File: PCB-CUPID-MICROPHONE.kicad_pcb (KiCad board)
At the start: 2 copper layers, 25.4 x 22.9 mm, 16 parts, among them J2 Conn_01x05

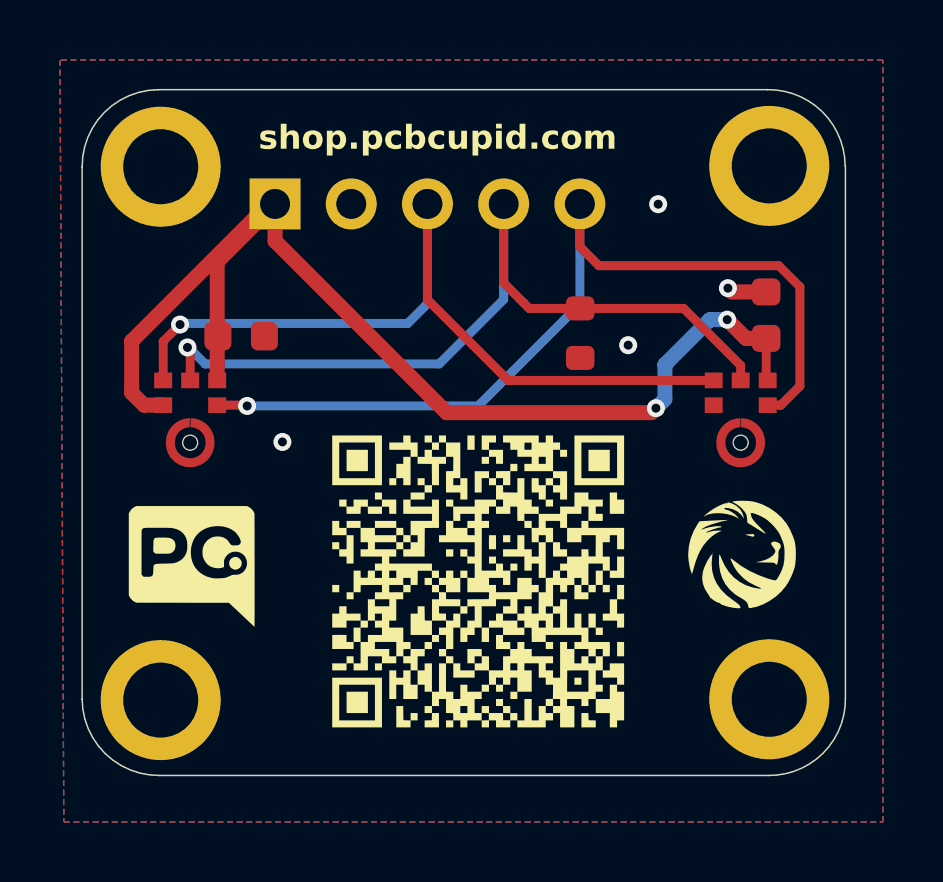
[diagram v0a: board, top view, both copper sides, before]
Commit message: updated pcbcupid-mic-2ch files
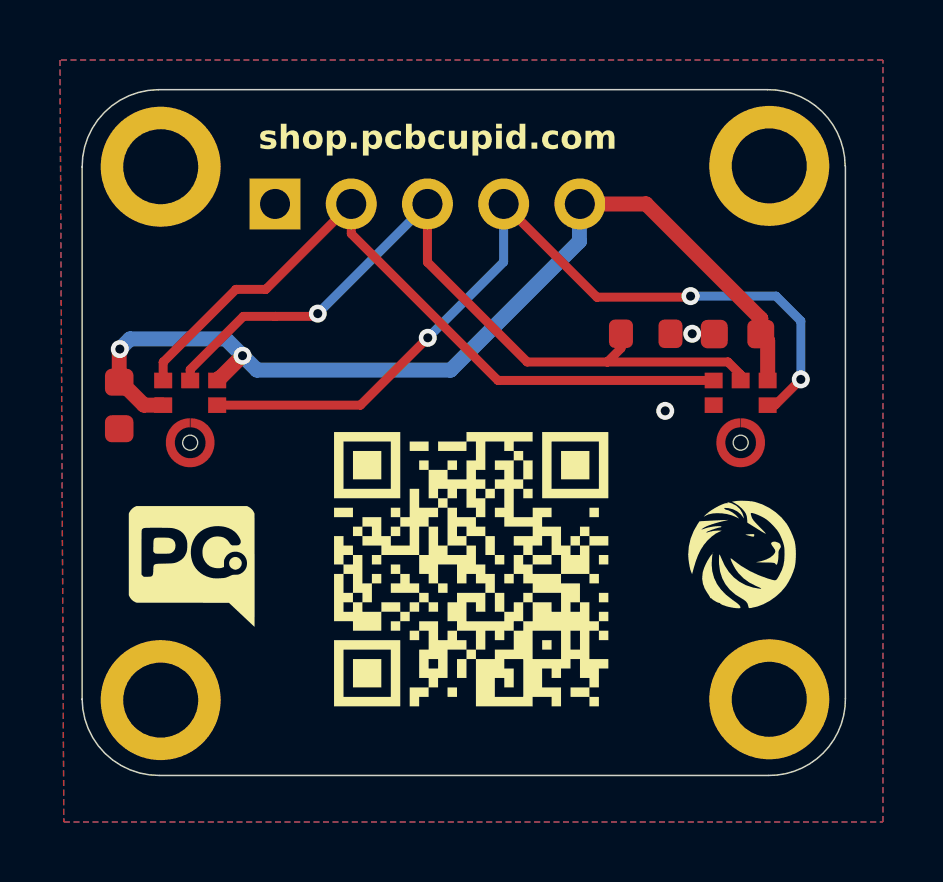
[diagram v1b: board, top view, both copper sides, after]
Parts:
- removed the G*** at (79.7, 109.1)
- moved C1 4.68 mm to (67.8, 103.2), turned to 90 degrees
- moved R1 2.19 mm to (85.3, 100.8), turned to 0 degrees
- moved C2 1.14 mm to (88.4, 100.8), turned to 180 degrees
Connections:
- J2 pad 1: +3.3V -> GND
- J2 pad 2: GND -> /WS
- J2 pad 3: /WS -> /SD
- J2 pad 4: /SD -> /SCK
- J2 pad 5: /SCK -> +3.3V
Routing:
- net +3.3V: track 39.9 -> 31.9 mm
- net /WS: track 27.9 -> 24.2 mm, vias 1 -> 0
- net /SCK: track 30.8 -> 28.4 mm, vias 1 -> 3
- net /SD: track 28.2 -> 25.8 mm
- net GND: track 1.33 -> 0.00 mm, vias 4 -> 2
